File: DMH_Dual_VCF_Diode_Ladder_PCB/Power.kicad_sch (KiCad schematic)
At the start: 14 parts, among them J0 Conn_01x01, J100 IDC_02x08, U1 TL074, U2 TL074

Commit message: Schematic design in progress
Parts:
- added U3: TL074, Package_DIP:DIP-14_W7.62mm_Socket, symbol Amplifier_Operational:TL074
- J0: now not fitted; now left out of the parts list
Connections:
- net Bus CV: now also U3.1; no longer J100.7a (Pin_7a), J100.7b (Pin_7b)
- new net: J100.7a (Pin_7a), J100.7b (Pin_7b)
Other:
- note removed: "Delete what's not needed!"
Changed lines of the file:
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@@
+	(wire
+		(pts
+			(xy 109.22 177.8) (xy 120.65 177.8)
+		)
+		(stroke
+			(width 0)
+			(type default)
+		)
+	)
 	(wire
 		(pts
@@
 		)
 	)
-	(text "Delete what's not needed!"
-		(exclude_from_sim yes)
-		(at 70.104 154.686 0)
+	(hierarchical_label "Bus Gate"
+		(shape output)
+		(at 36.83 193.04 0)
+		(fields_autoplaced yes)
 		(effects
 			(font
 				(size 1.27 1.27)
-				(thickness 0.254)
-				(bold yes)
-			)
-		)
-	)
-	(hierarchical_label "Bus Gate"
-		(shape output)
-		(at 36.83 193.04 0)
-		(fields_autoplaced yes)
-		(effects
-			(font
-				(size 1.27 1.27)
 			)
 			(justify left)
@@
 	(hierarchical_label "Bus CV"
 		(shape output)
-		(at 36.83 190.5 0)
+		(at 120.65 177.8 0)
 		(fields_autoplaced yes)
 		(effects
@@
 		(unit 1)
 		(exclude_from_sim no)
-		(in_bom yes)
+		(in_bom no)
 		(on_board yes)
-		(dnp no)
+		(dnp yes)
 		(property "Reference" "J0"
 			(at 147.32 177.8 90)
@@
 				)
 			)
+		)
+	)
+	(symbol
+		(lib_id "Amplifier_Operational:TL074")
+		(at 101.6 177.8 0)
+		(unit 1)
+		(exclude_from_sim no)
+		(in_bom yes)
+		(on_board yes)
+		(dnp no)
+		(fields_autoplaced yes)
+		(property "Reference" "U3"
+			(at 101.6 167.64 0)
+			(effects
+				(font
+					(size 1.27 1.27)
+				)
+			)
+		)
+		(property "Value" "TL074"
+			(at 101.6 170.18 0)
+			(effects
+				(font
+					(size 1.27 1.27)
+				)
+			)
+		)
+		(property "Footprint" "Package_DIP:DIP-14_W7.62mm_Socket"
+			(at 100.33 175.26 0)
+			(effects
+				(font
+					(size 1.27 1.27)
+				)
+				(hide yes)
+			)
+		)
+		(property "Datasheet" "http://www.ti.com/lit/ds/symlink/tl071.pdf"
+			(at 102.87 172.72 0)
+			(effects
+				(font
+					(size 1.27 1.27)
+				)
+				(hide yes)
+			)
+		)
+		(property "Description" "Quad Low-Noise JFET-Input Operational Amplifiers, DIP-14/SOIC-14"
+			(at 101.6 177.8 0)
+			(effects
+				(font
+					(size 1.27 1.27)
+				)
+				(hide yes)
+			)
+		)
+		(pin "1"
+		)
+		(pin "2"
+		)
+		(pin "10"
+		)
+		(pin "12"
+		)
+		(pin "7"
+		)
+		(pin "13"
+		)
+		(pin "11"
+		)
+		(pin "8"
+		)
+		(pin "5"
+		)
+		(pin "9"
+		)
+		(pin "4"
+		)
+		(pin "6"
+		)
+		(pin "3"
+		)
+		(pin "14"
+		)
+		(instances
+			(project ""
+				(path "/58f4306d-5387-4983-bb08-41a2313fd315/0cdf34b2-39cd-4d9e-981a-97cd34791509"
+					(reference "U3")
+					(unit 1)
+				)
+			)

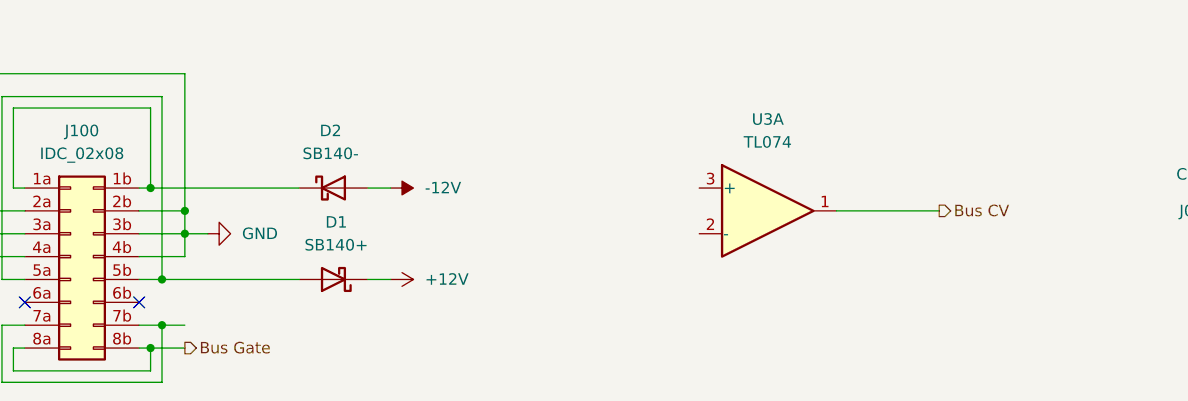
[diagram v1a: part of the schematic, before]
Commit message: Added Bus CV buffering
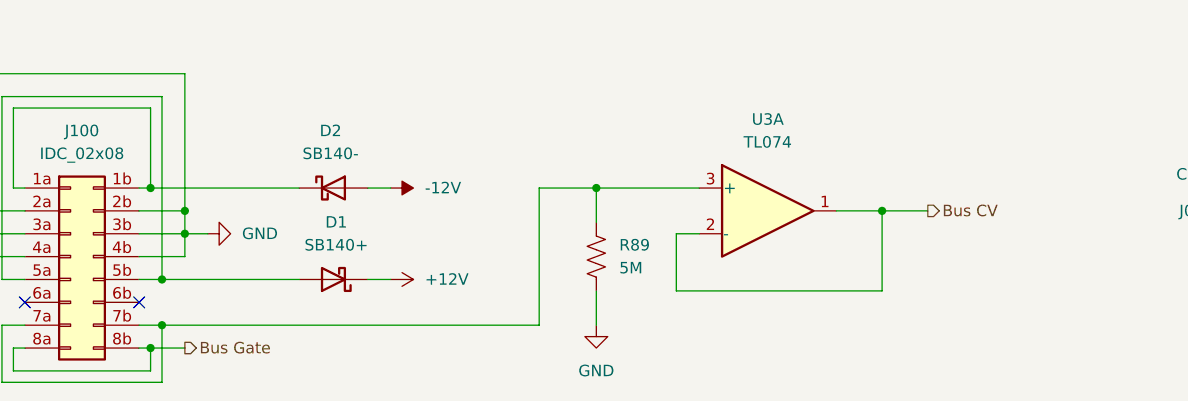
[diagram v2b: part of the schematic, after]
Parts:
- added R89: 5M, Resistor_THT:R_Axial_DIN0207_L6.3mm_D2.5mm_P7.62mm_Horizontal, symbol Device:R_US
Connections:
- net Bus CV: now also U3.2 (-)
- net GND: now also R89.2
- net at U3.3 (+): now also J100.7a (Pin_7a), J100.7b (Pin_7b), R89.1
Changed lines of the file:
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@@
+	)
+	(junction
+		(at 114.3 177.8)
+		(diameter 0)
+		(color 0 0 0 0)
 	)
 	(junction
@@
 	)
 	(junction
+		(at 82.55 175.26)
+		(diameter 0)
+		(color 0 0 0 0)
+	)
+	(junction
 		(at 88.9 146.05)
 		(diameter 0)
@@
 	(wire
 		(pts
+			(xy 114.3 186.69) (xy 114.3 177.8)
+		)
+		(stroke
+			(width 0)
+			(type default)
+		)
+	)
+	(wire
+		(pts
 			(xy 63.5 101.6) (xy 76.2 101.6)
 		)
@@
 	(wire
 		(pts
-			(xy 109.22 177.8) (xy 120.65 177.8)
+			(xy 109.22 177.8) (xy 114.3 177.8)
 		)
 		(stroke
@@
 	(wire
 		(pts
+			(xy 82.55 186.69) (xy 82.55 190.5)
+		)
+		(stroke
+			(width 0)
+			(type default)
+		)
+	)
+	(wire
+		(pts
 			(xy 88.9 101.6) (xy 88.9 113.03)
 		)
@@
 	(wire
 		(pts
+			(xy 91.44 186.69) (xy 114.3 186.69)
+		)
+		(stroke
+			(width 0)
+			(type default)
+		)
+	)
+	(wire
+		(pts
 			(xy 31.75 193.04) (xy 33.02 193.04)
 		)
@@
 	(wire
 		(pts
+			(xy 93.98 180.34) (xy 91.44 180.34)
+		)
+		(stroke
+			(width 0)
+			(type default)
+		)
+	)
+	(wire
+		(pts
 			(xy 21.59 95.25) (xy 34.29 95.25)
 		)
@@
 	(wire
 		(pts
-			(xy 34.29 190.5) (xy 36.83 190.5)
+			(xy 82.55 175.26) (xy 93.98 175.26)
+		)
+		(stroke
+			(width 0)
+			(type default)
+		)
+	)
+	(wire
+		(pts
+			(xy 34.29 190.5) (xy 76.2 190.5)
 		)
 		(stroke
@@
 	(wire
 		(pts
+			(xy 76.2 190.5) (xy 76.2 175.26)
+		)
+		(stroke
+			(width 0)
+			(type default)
+		)
+	)
+	(wire
+		(pts
 			(xy 16.51 165.1) (xy 34.29 165.1)
 		)
@@
 	(wire
 		(pts
+			(xy 76.2 175.26) (xy 82.55 175.26)
+		)
+		(stroke
+			(width 0)
+			(type default)
+		)
+	)
+	(wire
+		(pts
+			(xy 91.44 180.34) (xy 91.44 186.69)
+		)
+		(stroke
+			(width 0)
+			(type default)
+		)
+	)
+	(wire
+		(pts
 			(xy 101.6 139.7) (xy 88.9 139.7)
 		)
@@
 	(wire
 		(pts
+			(xy 82.55 175.26) (xy 82.55 179.07)
+		)
+		(stroke
+			(width 0)
+			(type default)
+		)
+	)
+	(wire
+		(pts
 			(xy 33.02 175.26) (xy 49.53 175.26)
 		)
@@
 		(pts
 			(xy 34.29 146.05) (xy 63.5 146.05)
+		)
+		(stroke
+			(width 0)
+			(type default)
+		)
+	)
+	(wire
+		(pts
+			(xy 114.3 177.8) (xy 119.38 177.8)
 		)
 		(stroke
@@
 	(hierarchical_label "Bus CV"
 		(shape output)
-		(at 120.65 177.8 0)
+		(at 119.38 177.8 0)
 		(fields_autoplaced yes)
 		(effects
@@
 	)
 	(symbol
+		(lib_id "power:GND")
+		(at 82.55 190.5 0)
+		(unit 1)
+		(exclude_from_sim no)
+		(in_bom yes)
+		(on_board yes)
+		(dnp no)
+		(fields_autoplaced yes)
+		(property "Reference" "#PWR073"
+			(at 82.55 196.85 0)
+			(effects
+				(font
+					(size 1.27 1.27)
+				)
+				(hide yes)
+			)
+		)
+		(property "Value" "GND"
+			(at 82.55 195.58 0)
+			(effects
+				(font
+					(size 1.27 1.27)
+				)
+			)
+		)
+		(property "Footprint" ""
+			(at 82.55 190.5 0)
+			(effects
+				(font
+					(size 1.27 1.27)
+				)
+				(hide yes)
+			)
+		)
+		(property "Datasheet" ""
+			(at 82.55 190.5 0)
+			(effects
+				(font
+					(size 1.27 1.27)
+				)
+				(hide yes)
+			)
+		)
+		(property "Description" "Power symbol creates a global label with name \"GND\" , ground"
+			(at 82.55 190.5 0)
+			(effects
+				(font
+					(size 1.27 1.27)
+				)
+				(hide yes)
+			)
+		)
+		(pin "1"
+		)
+		(instances
+			(project "DMH_Dual_VCF_Diode_Ladder_PCB"
+				(path "/58f4306d-5387-4983-bb08-41a2313fd315/0cdf34b2-39cd-4d9e-981a-97cd34791509"
+					(reference "#PWR073")
+					(unit 1)
+				)
+			)
+		)
+	)
+	(symbol
 		(lib_id "Device:C")
 		(at 34.29 133.35 0)
@@
 				(path "/58f4306d-5387-4983-bb08-41a2313fd315/0cdf34b2-39cd-4d9e-981a-97cd34791509"
 					(reference "D1")
+					(unit 1)
+				)
+			)
+		)
+	)
+	(symbol
+		(lib_id "Device:R_US")
+		(at 82.55 182.88 0)
+		(unit 1)
+		(exclude_from_sim no)
+		(in_bom yes)
+		(on_board yes)
+		(dnp no)
+		(fields_autoplaced yes)
+		(property "Reference" "R89"
+			(at 85.09 181.6099 0)
+			(effects
+				(font
+					(size 1.27 1.27)
+				)
+				(justify left)
+			)
+		)
+		(property "Value" "5M"
+			(at 85.09 184.1499 0)
+			(effects
+				(font
+					(size 1.27 1.27)
+				)
+				(justify left)
+			)
+		)
+		(property "Footprint" "Resistor_THT:R_Axial_DIN0207_L6.3mm_D2.5mm_P7.62mm_Horizontal"
+			(at 83.566 183.134 90)
+			(effects
+				(font
+					(size 1.27 1.27)
+				)
+				(hide yes)
+			)
+		)
+		(property "Datasheet" "~"
+			(at 82.55 182.88 0)
+			(effects
+				(font
+					(size 1.27 1.27)
+				)
+				(hide yes)
+			)
+		)
+		(property "Description" "Resistor, US symbol"
+			(at 82.55 182.88 0)
+			(effects
+				(font
+					(size 1.27 1.27)
+				)
+				(hide yes)
+			)
+		)
+		(pin "2"
+		)
+		(pin "1"
+		)
+		(instances
+			(project "DMH_Dual_VCF_Diode_Ladder_PCB"
+				(path "/58f4306d-5387-4983-bb08-41a2313fd315/0cdf34b2-39cd-4d9e-981a-97cd34791509"
+					(reference "R89")
 					(unit 1)
 				)
@@
 		(on_board yes)
 		(dnp no)
-		(fields_autoplaced yes)
 		(property "Reference" "U3"
 			(at 101.6 167.64 0)

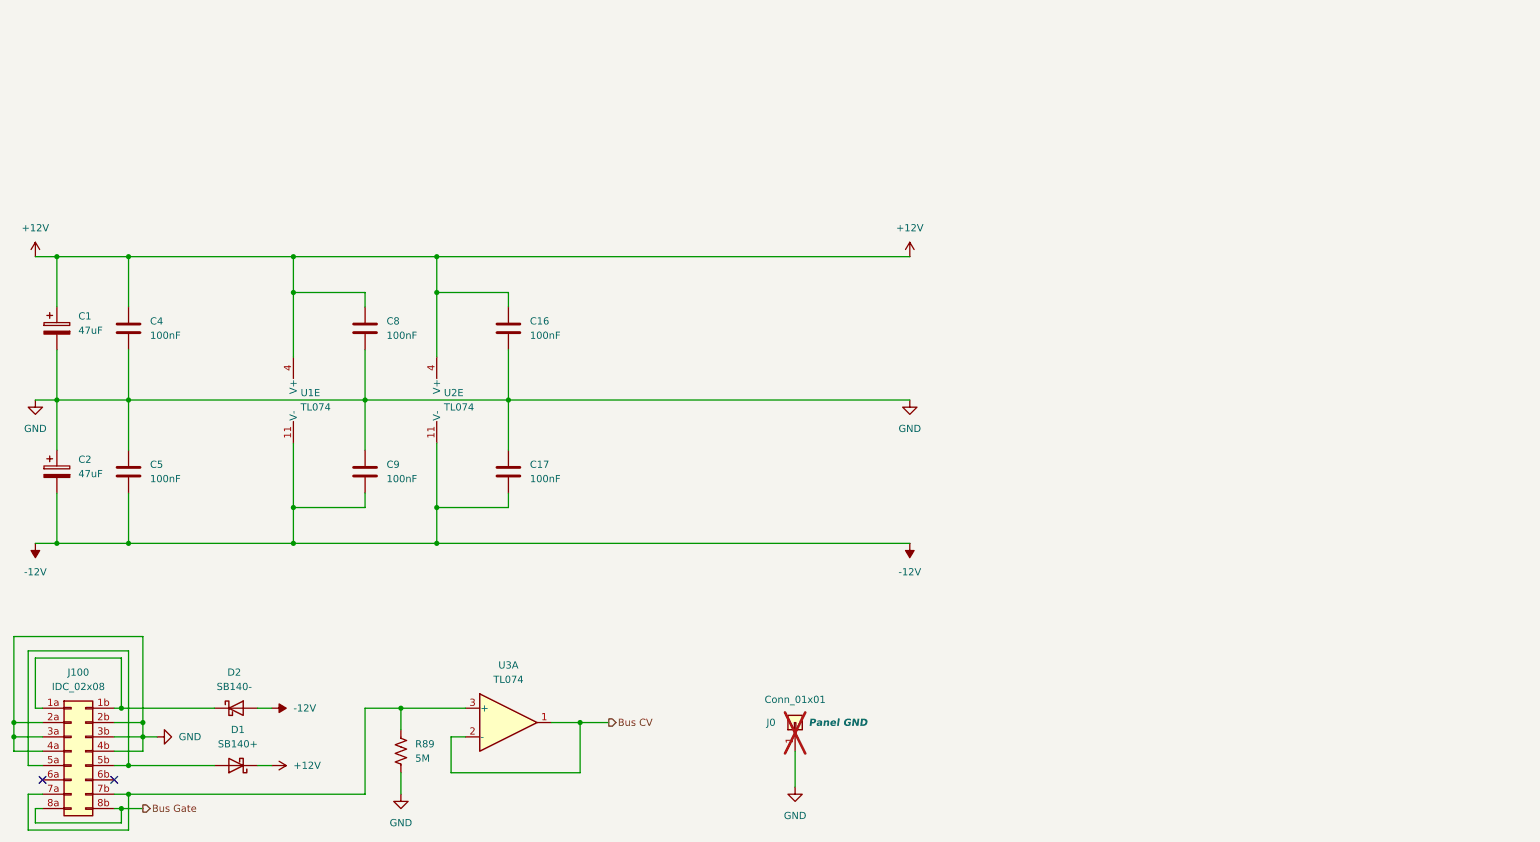
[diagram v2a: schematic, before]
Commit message: Reannotated whole schematic
OpAmp annotation is still tentative.
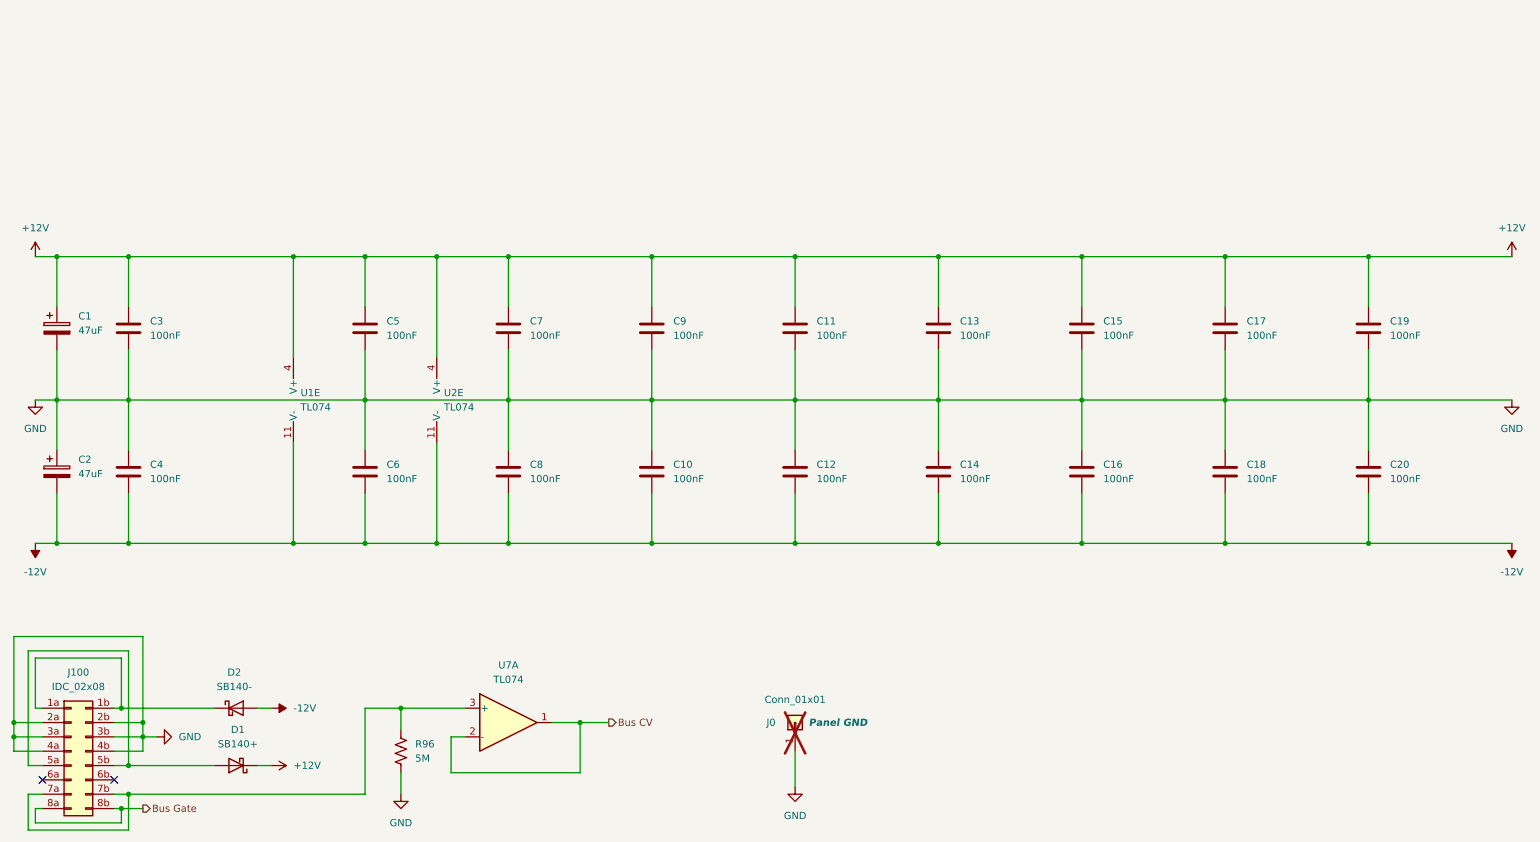
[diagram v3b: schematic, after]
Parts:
- added C10, C11, C12, C13, C14, C15, C16, C17, C18, C19, C20, C9: 100nF, Capacitor_THT:C_Disc_D4.3mm_W1.9mm_P5.00mm, symbol Device:C
- renumbered C4 to C3, C5 to C4, C8 to C5, C9 to C6, C16 to C7, C17 to C8, R89 to R96, U3 to U7
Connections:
- net +12V: now also C11.1, C13.1, C15.1, C17.1, C19.1, C9.1
- net -12V: now also C10.2, C12.2, C14.2, C16.2, C18.2, C20.2
- net GND: now also C10.1, C11.2, C12.1, C13.2, C14.1, C15.2, C16.1, C17.2, C18.1, C19.2, C20.1, C9.2

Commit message: Reannotated OpAmps and cleared errors
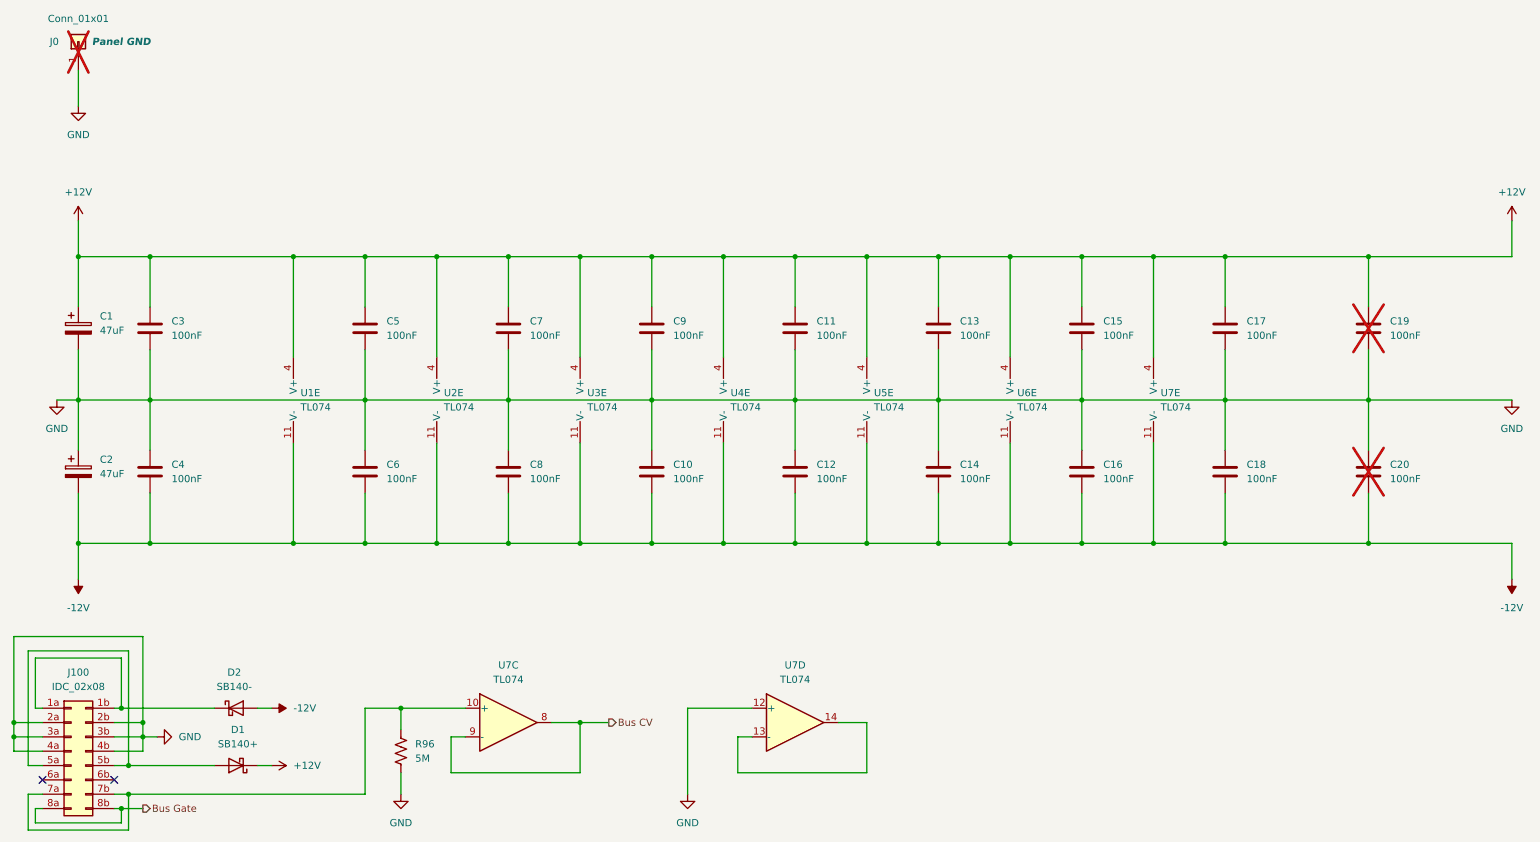
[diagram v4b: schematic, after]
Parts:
- added U3: TL074, Package_DIP:DIP-14_W7.62mm_Socket, symbol Amplifier_Operational:TL074
- added U4, U5, U6: TL074, symbol Amplifier_Operational:TL074
- added unit 4 of U7
- added unit 5 of U7
- C19, C20: now not fitted; now left out of the parts list
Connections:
- net +12V: now also U3.4 (V+), U4.4 (V+), U5.4 (V+), U6.4 (V+), U7.4 (V+)
- net -12V: now also U3.11 (V-), U4.11 (V-), U5.11 (V-), U6.11 (V-), U7.11 (V-)
- net Bus CV: now also U7.8, U7.9 (-); no longer U7.1, U7.2 (-)
- net GND: now also U7.12 (+)
- net at J100.7a (Pin_7a), J100.7b (Pin_7b), R96.1: now also U7.10 (+); no longer U7.3 (+)
- new net: U7.13 (-), U7.14
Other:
- moved on the sheet: C1, C2, C3, C4, J0

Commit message: Updated switches symbols and fps
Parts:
- U4, U5, U6, U7: footprint (none) -> Package_DIP:DIP-14_W7.62mm_Socket
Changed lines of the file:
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@@
 			)
 		)
-		(property "Footprint" ""
+		(property "Footprint" "Package_DIP:DIP-14_W7.62mm_Socket"
 			(at 166.37 118.11 0)
 			(effects
@@
 			)
 		)
-		(property "Footprint" ""
+		(property "Footprint" "Package_DIP:DIP-14_W7.62mm_Socket"
 			(at 151.13 175.26 0)
 			(effects
@@
 			)
 		)
-		(property "Footprint" ""
+		(property "Footprint" "Package_DIP:DIP-14_W7.62mm_Socket"
 			(at 140.97 118.11 0)
 			(effects
@@
 			)
 		)
-		(property "Footprint" ""
+		(property "Footprint" "Package_DIP:DIP-14_W7.62mm_Socket"
 			(at 217.17 118.11 0)
 			(effects
@@
 			)
 		)
-		(property "Footprint" ""
+		(property "Footprint" "Package_DIP:DIP-14_W7.62mm_Socket"
 			(at 191.77 118.11 0)
 			(effects
